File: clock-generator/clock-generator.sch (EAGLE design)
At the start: 100 parts, among them IC1 24C00TS, K2 694108106102, M1 MENTOR_12701001, U1 SN74LVC1G04DBV, U2 ADP151AUJZ, U3 ATSAMD11-QFN24, U4 SI5351C, U5 IP4234CZ6, U6 IP4234CZ6, X1 MINI-USB-SHIELD-UX60A-MB-5ST, X2 JACK2.5_SJ-2523, X4 UEXT/90

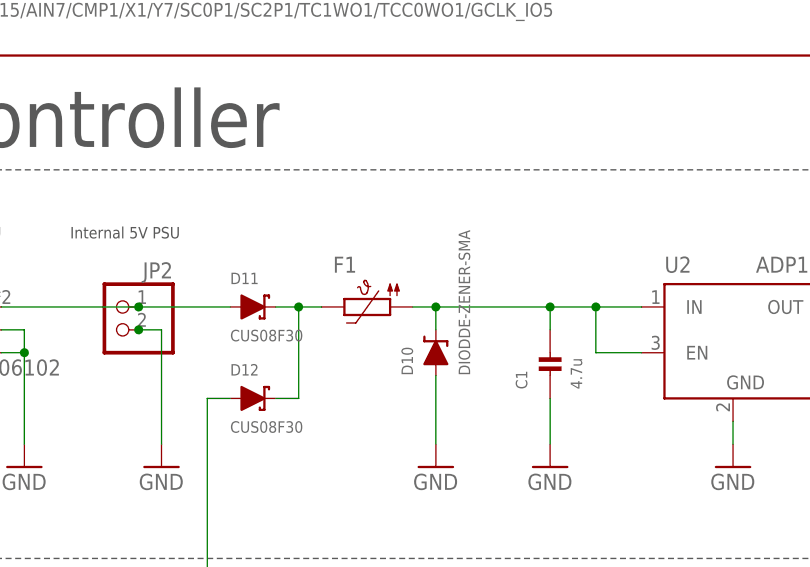
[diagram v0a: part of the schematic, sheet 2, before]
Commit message: clock-gen: Add BOM information + PDF exports of schematics
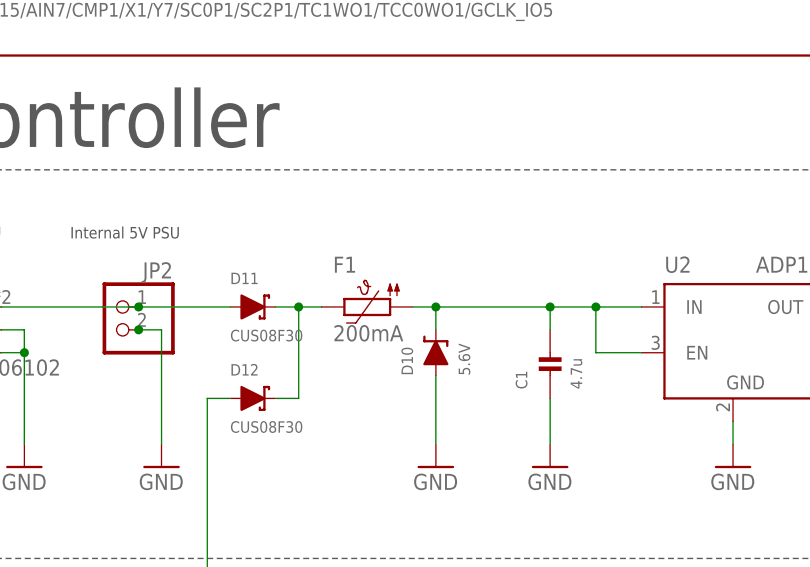
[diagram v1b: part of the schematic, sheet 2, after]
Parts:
- C1, C14, C15: CLASS (none) -> CAPACITOR; DESCRIPTION (none) -> CAP CER 4.7UF 16V X5R 0805; LINK (none) -> https://www.digikey.de/product-detail/de/samsung-electro-me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; MANUFACTURER (none) -> Samsung Electro-Mechanics; MANUFACTURERPARTNUMBER (none) -> CL21A475KOFNNNE; POPULATED (none) -> TRUE; ROHSCERTIFICATE (none) -> Bleifrei / RoHS-konform; SOURCE (none) -> DIGIKEY; SOURCEPARTNUMBER (none) -> 1276-1065-1-ND
- C10, C11, C12, C13, C8: CLASS (none) -> CAPACITOR; DESCRIPTION (none) -> CAP CER 10000PF 25V X7R 0402; LINK (none) -> https://www.digikey.de/product-detail/de/samsung-electro-me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; MANUFACTURER (none) -> Samsung Electro-Mechanics; MANUFACTURERPARTNUMBER (none) -> CL05B103KA5NNNC; POPULATED (none) -> TRUE; ROHSCERTIFICATE (none) -> Bleifrei / RoHS-konform; SOURCE (none) -> DIGIKEY; SOURCEPARTNUMBER (none) -> 1276-1057-1-ND
- C16, C17, C18, C19, C2, C20, C21, C22, C23, C24, C25, C26, C27, C28, C6, C7, C9: CLASS (none) -> CAPACITOR; DESCRIPTION (none) -> CAP CER 0.1UF 16V X7R 0603; LINK (none) -> https://www.digikey.de/product-detail/de/samsung-electro-me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; MANUFACTURER (none) -> Samsung Electro-Mechanics; MANUFACTURERPARTNUMBER (none) -> CL10B104KO8NNNC; POPULATED (none) -> TRUE; ROHSCERTIFICATE (none) -> Bleifrei / RoHS-konform; SOURCE (none) -> DIGIKEY; SOURCEPARTNUMBER (none) -> 1276-1005-1-ND
- C3: CLASS (none) -> CAPACITOR; DESCRIPTION (none) -> CAP CER 0.1UF 10V X5R 0402; LINK (none) -> https://www.digikey.de/product-detail/de/samsung-electro-me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; MANUFACTURER (none) -> Samsung Electro-Mechanics; MANUFACTURERPARTNUMBER (none) -> CL05A104MP5NNNC; POPULATED (none) -> TRUE; ROHSCERTIFICATE (none) -> Bleifrei / RoHS-konform; SOURCE (none) -> DIGIKEY; SOURCEPARTNUMBER (none) -> 1276-1443-1-ND
- C4: CLASS (none) -> CAPACITOR; DESCRIPTION (none) -> CAP CER 1UF 10V X5R 0603; LINK (none) -> https://www.digikey.de/product-detail/de/samsung-electro-me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; MANUFACTURER (none) -> Samsung Electro-Mechanics; MANUFACTURERPARTNUMBER (none) -> CL10A105KP8NNNC; POPULATED (none) -> TRUE; ROHSCERTIFICATE (none) -> Bleifrei / RoHS-konform; SOURCE (none) -> DIGIKEY; SOURCEPARTNUMBER (none) -> 1276-1182-1-ND
- C5: value 0.10n -> 10n; CLASS (none) -> CAPACITOR; DESCRIPTION (none) -> CAP CER 10000PF 25V X7R 0402; LINK (none) -> https://www.digikey.de/product-detail/de/samsung-electro-me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; MANUFACTURER (none) -> Samsung Electro-Mechanics; MANUFACTURERPARTNUMBER (none) -> CL05B103KA5NNNC; POPULATED (none) -> TRUE; ROHSCERTIFICATE (none) -> Bleifrei / RoHS-konform; SOURCE (none) -> DIGIKEY; SOURCEPARTNUMBER (none) -> 1276-1057-1-ND
- C701: DESCRIPTION CAP CER 10000PF 50V X7R 0402 -> CAP CER 10000PF 25V X7R 0402; LINK https://www.digikey.de/product-detail/de/avx-corporation/04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 -> https://www.digikey.de/product-detail/de/samsung-electro-me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; MANUFACTURER AVX Corporation -> Samsung Electro-Mechanics; MANUFACTURERPARTNUMBER 04025C103KAT2A -> CL05B103KA5NNNC; SOURCEPARTNUMBER 478-7882-1-ND -> 1276-1057-1-ND
- CLK0, CLK1, CLK2, CLK3, CLK4, CLK5, CLK6, CLK7, CLKIN: CLASS (none) -> CAPACITOR; DESCRIPTION (none) -> CONN SMA JACK R/A 50 OHM PCB; LINK (none) -> https://www.digikey.de/product-detail/de/te-connectivity-am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; MANUFACTURER (none) -> TE Connectivity AMP Connectors; MANUFACTURERPARTNUMBER (none) -> 619540-1; POPULATED (none) -> FALSE; ROHSCERTIFICATE (none) -> Bleifrei / RoHS-konform; SOURCE (none) -> DIGIKEY; SOURCEPARTNUMBER (none) -> A120734-ND
- CLK0U, CLK1U, CLK2U, CLK3U, CLK4U, CLK5U, CLK6U, CLK7U, CLKINU: CLASS (none) -> CAPACITOR; DESCRIPTION (none) -> CONN U.FL RCPT STR 50 OHM SMD; LINK (none) -> https://www.digikey.de/product-detail/de/hirose-electric-co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; MANUFACTURER (none) -> Hirose Electric Co Ltd; MANUFACTURERPARTNUMBER (none) -> U.FL-R-SMT(10); POPULATED (none) -> TRUE; ROHSCERTIFICATE (none) -> Bleifrei / RoHS-konform; SOURCE (none) -> DIGIKEY; SOURCEPARTNUMBER (none) -> H9161CT-ND
- D1, D2, D3, D4, D5, D6, D7, D8, D9: CLASS (none) -> DIODE; DESCRIPTION (none) -> SUPPRESSOR ESD 30VDC 0603 SMD; LINK (none) -> https://www.digikey.de/product-detail/de/eaton-electronics-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; MANUFACTURER (none) -> Eaton - Electronics Division; MANUFACTURERPARTNUMBER (none) -> 0603ESDA2-TR2; POPULATED (none) -> TRUE; ROHSCERTIFICATE (none) -> Bleifrei / RoHS-konform; SOURCE (none) -> DIGIKEY; SOURCEPARTNUMBER (none) -> 283-4156-1-ND
- D10: value DIODDE-ZENER-SMA -> 5.6V; CLASS (none) -> DIODE; DESCRIPTION (none) -> DIODE ZENER 5.6V 3W DO214AC; LINK (none) -> https://www.digikey.de/product-detail/de/micro-commercial-c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; MANUFACTURER (none) -> Micro Commercial Co; MANUFACTURERPARTNUMBER (none) -> 3SMAJ5919B-TP; POPULATED (none) -> TRUE; ROHSCERTIFICATE (none) -> Bleifrei / RoHS-konform; SOURCE (none) -> DIGIKEY; SOURCEPARTNUMBER (none) -> 3SMAJ5919B-TPMSCT-ND
- D11, D12: CLASS (none) -> DIODE; DESCRIPTION (none) -> DIODE SCHOTTKY 30V 800MA USC; LINK (none) -> https://www.digikey.de/product-detail/de/toshiba-semiconduc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; MANUFACTURER (none) -> Toshiba Semiconductor and Storage; MANUFACTURERPARTNUMBER (none) -> CUS08F30,H3F; POPULATED (none) -> TRUE; ROHSCERTIFICATE (none) -> Bleifrei / RoHS-konform; SOURCE (none) -> DIGIKEY; SOURCEPARTNUMBER (none) -> CUS08F30H3FCT-ND
- F1: value (none) -> 200mA; CLASS (none) -> UNKNOWN CLASS; DESCRIPTION (none) -> PTC RESET FUSE 30V 200MA 1206; LINK (none) -> https://www.digikey.de/product-detail/de/0ZCJ0020FF2E/507-1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; MANUFACTURER (none) -> Bel Fuse Inc.; MANUFACTURERPARTNUMBER (none) -> 0ZCJ0020FF2E; POPULATED (none) -> TRUE; ROHSCERTIFICATE (none) -> Bleifrei / RoHS-konform; SOURCE (none) -> DIGIKEY; SOURCEPARTNUMBER (none) -> 507-1797-1-ND
- IC1: CLASS (none) -> UNKNOWN CLASS; DESCRIPTION (none) -> IC EEPROM 2K I2C 1MHZ 8TSSOP; LINK (none) -> https://www.digikey.de/product-detail/de/microchip-technolo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; MANUFACTURER (none) -> Microchip Technology; MANUFACTURERPARTNUMBER (none) -> AT24C02C-XHM-T; POPULATED (none) -> TRUE; ROHSCERTIFICATE (none) -> Bleifrei / RoHS-konform; SOURCE (none) -> DIGIKEY; SOURCEPARTNUMBER (none) -> AT24C02C-XHM-TCT-ND
- JP1, JP2: CLASS (none) -> CONNECTOR\JUMPER; DESCRIPTION (none) -> CONN HEADER VERT 2POS 2.54MM; LINK (none) -> https://www.digikey.de/product-detail/de/PREC002SAAN-RC/S10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; MANUFACTURER (none) -> Sullins Connector Solutions; MANUFACTURERPARTNUMBER (none) -> PREC002SAAN-RC; POPULATED (none) -> TRUE; ROHSCERTIFICATE (none) -> Bleifrei / RoHS-konform; SOURCE (none) -> DIGIKEY; SOURCEPARTNUMBER (none) -> S1012EC-02-ND
- K2: DESCRIPTION Power Barrel Connector Jack 2.50mm ID (0.098"), 5.50mm OD (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 -> CONN PWR JACK 2.5X5.5MM SOLDER; LINK http://www.digikey.com/product-detail/en/wurth-electronics-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 -> http://www.digikey.de/product-detail/de/wurth-electronics-i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; MANUFACTURER Wurth Electronics Inc -> Wurth Electronics Inc.; ROHSCERTIFICATE UNKNOWN ROHS CERTIFICATE -> Bleifrei / RoHS-konform
- L2: CLASS (none) -> INDUCTOR; DESCRIPTION (none) -> FERRITE BEAD 1 KOHM 0805 1LN; LINK (none) -> https://www.digikey.de/product-detail/de/wurth-electronics-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; MANUFACTURER (none) -> Wurth Electronics Inc.; MANUFACTURERPARTNUMBER (none) -> 742792096; POPULATED (none) -> TRUE; ROHSCERTIFICATE (none) -> Bleifrei / RoHS-konform; SOURCE (none) -> DIGIKEY; SOURCEPARTNUMBER (none) -> 732-4648-1-ND
- LED1: CLASS (none) -> LED; DESCRIPTION (none) -> LED GREEN CLEAR 2PLCC SMD; LINK (none) -> https://www.digikey.de/product-detail/de/osram-opto-semicon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; MANUFACTURER (none) -> OSRAM Opto Semiconductors Inc.; MANUFACTURERPARTNUMBER (none) -> LG T67F-R1T1-24; POPULATED (none) -> TRUE; ROHSCERTIFICATE (none) -> Bleifrei / RoHS-konform; SOURCE (none) -> DIGIKEY; SOURCEPARTNUMBER (none) -> 475-3413-1-ND
- LED2: CLASS (none) -> LED; DESCRIPTION (none) -> LED YELLOW CLEAR 2PLCC SMD; LINK (none) -> https://www.digikey.de/product-detail/de/osram-opto-semicon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; MANUFACTURER (none) -> OSRAM Opto Semiconductors Inc.; MANUFACTURERPARTNUMBER (none) -> LY T676-S1T1-26-Z; POPULATED (none) -> TRUE; ROHSCERTIFICATE (none) -> Bleifrei / RoHS-konform; SOURCE (none) -> DIGIKEY; SOURCEPARTNUMBER (none) -> 475-2665-1-ND
- M1: CLASS (none) -> UNKNOWN CLASS; DESCRIPTION (none) -> NO DESCRIPTION; LINK (none) -> UNKNOWN LINK; MANUFACTURER (none) -> UNKNOWN MANUFACTURER; MANUFACTURERPARTNUMBER (none) -> UNKNOWN MANUFACTURER PART NUMBER; POPULATED (none) -> TRUE; ROHSCERTIFICATE (none) -> UNKNOWN ROHS CERTIFICATE; SOURCE (none) -> UNKNOWN SOURCE; SOURCEPARTNUMBER (none) -> UNKNOWN SOURCE PART NUMBER
- R1, R701, R703: DESCRIPTION RES 100K OHM 1/10W 1% 0603 SMD -> RES SMD 100K OHM 5%% 1/10W 0603; LINK http://www.digikey.de/product-detail/de/foo/RHM100KCFCT-ND -> https://www.digikey.de/product-detail/de/yageo/RC0603JR-071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; MANUFACTURER Rohm Semiconductor -> Yageo; MANUFACTURERPARTNUMBER MCR03ERTF1003 -> RC0603JR-07100KL; SOURCEPARTNUMBER RHM100KCFCT-ND -> 311-100KGRCT-ND
- R10, R11, R2, R3: CLASS (none) -> RESISTOR; DESCRIPTION (none) -> RES 1K OHM 1%% 1/10W 0603; LINK (none) -> https://www.digikey.de/product-detail/de/stackpole-electron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; MANUFACTURER (none) -> Stackpole Electronics Inc.; MANUFACTURERPARTNUMBER (none) -> RMCF0603FT1K00; POPULATED (none) -> TRUE; ROHSCERTIFICATE (none) -> Bleifrei / RoHS-konform; SOURCE (none) -> DIGIKEY; SOURCEPARTNUMBER (none) -> RMCF0603FT1K00CT-ND
- R12, R15: CLASS (none) -> RESISTOR; DESCRIPTION (none) -> RES 33 OHM 5%% 1/10W 0603; LINK (none) -> https://www.digikey.de/product-detail/de/stackpole-electron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; MANUFACTURER (none) -> Stackpole Electronics Inc.; MANUFACTURERPARTNUMBER (none) -> RMCF0603JT33R0; POPULATED (none) -> TRUE; ROHSCERTIFICATE (none) -> Bleifrei / RoHS-konform; SOURCE (none) -> DIGIKEY; SOURCEPARTNUMBER (none) -> RMCF0603JT33R0CT-ND
- R13, R14: DESCRIPTION RES 100K OHM 1/10W 1% 0603 SMD -> RES 330 OHM 5%% 1/10W 0603; LINK http://www.digikey.de/product-detail/de/foo/RHM100KCFCT-ND -> https://www.digikey.de/product-detail/de/stackpole-electron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; MANUFACTURER Rohm Semiconductor -> Stackpole Electronics Inc.; MANUFACTURERPARTNUMBER MCR03ERTF1003 -> RMCF0603JT330R; SOURCEPARTNUMBER RHM100KCFCT-ND -> RMCF0603JT330RCT-ND
- R16: DESCRIPTION RES 100K OHM 1/10W 1% 0603 SMD -> RES SMD 30K OHM 5%% 1/10W 0603; LINK http://www.digikey.de/product-detail/de/foo/RHM100KCFCT-ND -> https://www.digikey.de/product-detail/de/yageo/RC0603JR-073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; MANUFACTURER Rohm Semiconductor -> Yageo; MANUFACTURERPARTNUMBER MCR03ERTF1003 -> RC0603JR-0730KL; SOURCEPARTNUMBER RHM100KCFCT-ND -> 311-30KGRCT-ND
- R17: DESCRIPTION RES 100K OHM 1/10W 1% 0603 SMD -> RES SMD 47K OHM 5%% 1/10W 0603; LINK http://www.digikey.de/product-detail/de/foo/RHM100KCFCT-ND -> https://www.digikey.de/product-detail/de/yageo/RC0603JR-074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; MANUFACTURER Rohm Semiconductor -> Yageo; MANUFACTURERPARTNUMBER MCR03ERTF1003 -> RC0603JR-0747KL; SOURCEPARTNUMBER RHM100KCFCT-ND -> 311-47KGRCT-ND
- R4, R5, R6: CLASS (none) -> RESISTOR; DESCRIPTION (none) -> RES 10K OHM 5%% 1/10W 0603; LINK (none) -> https://www.digikey.de/product-detail/de/stackpole-electron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; MANUFACTURER (none) -> Stackpole Electronics Inc.; MANUFACTURERPARTNUMBER (none) -> RMCF0603JT10K0; POPULATED (none) -> TRUE; ROHSCERTIFICATE (none) -> Bleifrei / RoHS-konform; SOURCE (none) -> DIGIKEY; SOURCEPARTNUMBER (none) -> RMCF0603JT10K0CT-ND
- R7: CLASS (none) -> RESISTOR; DESCRIPTION (none) -> RES 49.9 OHM 1%% 1/10W 0603; LINK (none) -> https://www.digikey.de/product-detail/de/stackpole-electron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; MANUFACTURER (none) -> Stackpole Electronics Inc.; MANUFACTURERPARTNUMBER (none) -> RMCF0603FT49R9; POPULATED (none) -> TRUE; ROHSCERTIFICATE (none) -> Bleifrei / RoHS-konform; SOURCE (none) -> DIGIKEY; SOURCEPARTNUMBER (none) -> RMCF0603FT49R9CT-ND
- R8, R9: CLASS (none) -> RESISTOR; DESCRIPTION (none) -> RES SMD 510K OHM 1%% 1/10W 0603; LINK (none) -> https://www.digikey.de/product-detail/de/yageo/RC0603FR-075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; MANUFACTURER (none) -> Yageo; MANUFACTURERPARTNUMBER (none) -> RC0603FR-07510KL; POPULATED (none) -> TRUE; ROHSCERTIFICATE (none) -> Bleifrei / RoHS-konform; SOURCE (none) -> DIGIKEY; SOURCEPARTNUMBER (none) -> 311-510KHRCT-ND
- TC1: CLASS (none) -> UNKNOWN CLASS; DESCRIPTION (none) -> NO DESCRIPTION; LINK (none) -> UNKNOWN LINK; MANUFACTURER (none) -> UNKNOWN MANUFACTURER; MANUFACTURERPARTNUMBER (none) -> UNKNOWN MANUFACTURER PART NUMBER; POPULATED (none) -> FALSE; ROHSCERTIFICATE (none) -> UNKNOWN ROHS CERTIFICATE; SOURCE (none) -> UNKNOWN SOURCE; SOURCEPARTNUMBER (none) -> UNKNOWN SOURCE PART NUMBER
- U1: CLASS (none) -> IC; DESCRIPTION (none) -> IC INVERTER 1CH 1-INP SOT23-5; LINK (none) -> https://www.digikey.de/product-detail/de/texas-instruments/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; MANUFACTURER (none) -> Texas Instruments; MANUFACTURERPARTNUMBER (none) -> SN74LVC1G04DBVR; POPULATED (none) -> TRUE; ROHSCERTIFICATE (none) -> Bleifrei / RoHS-konform; SOURCE (none) -> DIGIKEY; SOURCEPARTNUMBER (none) -> 296-11599-1-ND
- U2: CLASS (none) -> IC; DESCRIPTION (none) -> IC REG LINEAR 3V 200MA TSOT5; LINK (none) -> https://www.digikey.de/product-detail/de/analog-devices-inc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; MANUFACTURER (none) -> Analog Devices Inc.; MANUFACTURERPARTNUMBER (none) -> ADP151AUJZ-3.0-R7; POPULATED (none) -> TRUE; ROHSCERTIFICATE (none) -> Bleifrei / RoHS-konform; SOURCE (none) -> DIGIKEY; SOURCEPARTNUMBER (none) -> ADP151AUJZ-3.0-R7CT-ND
- U3: CLASS (none) -> IC; DESCRIPTION (none) -> IC MCU 32BIT 16KB FLASH 24QFN; LINK (none) -> https://www.digikey.de/product-detail/de/microchip-technolo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; MANUFACTURER (none) -> Microchip Technology; MANUFACTURERPARTNUMBER (none) -> ATSAMD11D14A-MUT; POPULATED (none) -> TRUE; ROHSCERTIFICATE (none) -> Bleifrei / RoHS-konform; SOURCE (none) -> DIGIKEY; SOURCEPARTNUMBER (none) -> ATSAMD11D14A-MUTCT-ND
- U4: CLASS (none) -> IC; DESCRIPTION (none) -> IC CLK GENERATOR 200MHZ 20QFN; LINK (none) -> https://www.digikey.de/product-detail/de/silicon-labs/SI535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; MANUFACTURER (none) -> Silicon Labs; MANUFACTURERPARTNUMBER (none) -> SI5351C-B-GMR; POPULATED (none) -> TRUE; ROHSCERTIFICATE (none) -> Bleifrei / RoHS-konform; SOURCE (none) -> DIGIKEY; SOURCEPARTNUMBER (none) -> 336-5160-6-ND
- U5, U6: CLASS (none) -> IC; DESCRIPTION (none) -> TVS DIODE 5.5V 6TSOP; LINK (none) -> https://www.digikey.de/product-detail/de/nexperia-usa-inc/I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; MANUFACTURER (none) -> Nexperia USA Inc.; MANUFACTURERPARTNUMBER (none) -> IP4234CZ6,125; POPULATED (none) -> TRUE; ROHSCERTIFICATE (none) -> Bleifrei / RoHS-konform; SOURCE (none) -> DIGIKEY; SOURCEPARTNUMBER (none) -> 1727-4717-1-ND
- X1: CLASS (none) -> CONNECTOR; DESCRIPTION (none) -> CONN RCPT USB2.0 MINI B SMD R/A; LINK (none) -> https://www.digikey.de/product-detail/de/hirose-electric-co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; MANUFACTURER (none) -> Hirose Electric Co Ltd; MANUFACTURERPARTNUMBER (none) -> UX60A-MB-5ST; POPULATED (none) -> TRUE; ROHSCERTIFICATE (none) -> Bleifrei / RoHS-konform; SOURCE (none) -> DIGIKEY; SOURCEPARTNUMBER (none) -> H2961CT-ND
- X2: CLASS (none) -> CONNECTOR; DESCRIPTION (none) -> CONN JACK STEREO 2.5MM SMD R/A; LINK (none) -> https://www.digikey.de/product-detail/de/cui-inc/SJ-2523-SM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; MANUFACTURER (none) -> CUI Inc.; MANUFACTURERPARTNUMBER (none) -> SJ-2523-SMT-TR; POPULATED (none) -> TRUE; ROHSCERTIFICATE (none) -> Bleifrei / RoHS-konform; SOURCE (none) -> DIGIKEY; SOURCEPARTNUMBER (none) -> CP-2523SJCT-ND
- X3: CLASS (none) -> CONNECTOR; DESCRIPTION (none) -> NO DESCRIPTION; LINK (none) -> UNKNOWN LINK; MANUFACTURER (none) -> UNKNOWN MANUFACTURER; MANUFACTURERPARTNUMBER (none) -> UNKNOWN MANUFACTURER PART NUMBER; POPULATED (none) -> FALSE; ROHSCERTIFICATE (none) -> UNKNOWN ROHS CERTIFICATE; SOURCE (none) -> UNKNOWN SOURCE; SOURCEPARTNUMBER (none) -> UNKNOWN SOURCE PART NUMBER
- X4: CLASS (none) -> CONNECTOR; DESCRIPTION (none) -> CONN HEADER VERT 10POS 2.54MM; LINK (none) -> https://www.digikey.de/product-detail/de/on-shore-technolog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; MANUFACTURER (none) -> On Shore Technology Inc.; MANUFACTURERPARTNUMBER (none) -> 302-S101; POPULATED (none) -> TRUE; ROHSCERTIFICATE (none) -> Bleifrei / RoHS-konform; SOURCE (none) -> DIGIKEY; SOURCEPARTNUMBER (none) -> ED1543-ND
- XO1: CLASS (none) -> CONNECTOR; DESCRIPTION (none) -> XTAL OSC VCTCXO 10.0000MHZ LVCMO; LINK (none) -> https://www.digikey.de/product-detail/de/connor-winfield/T6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; MANUFACTURER (none) -> Connor-Winfield; MANUFACTURERPARTNUMBER (none) -> T604-010.0M; POPULATED (none) -> TRUE; ROHSCERTIFICATE (none) -> Bleifrei / RoHS-konform; SOURCE (none) -> DIGIKEY; SOURCEPARTNUMBER (none) -> CW769CT-ND

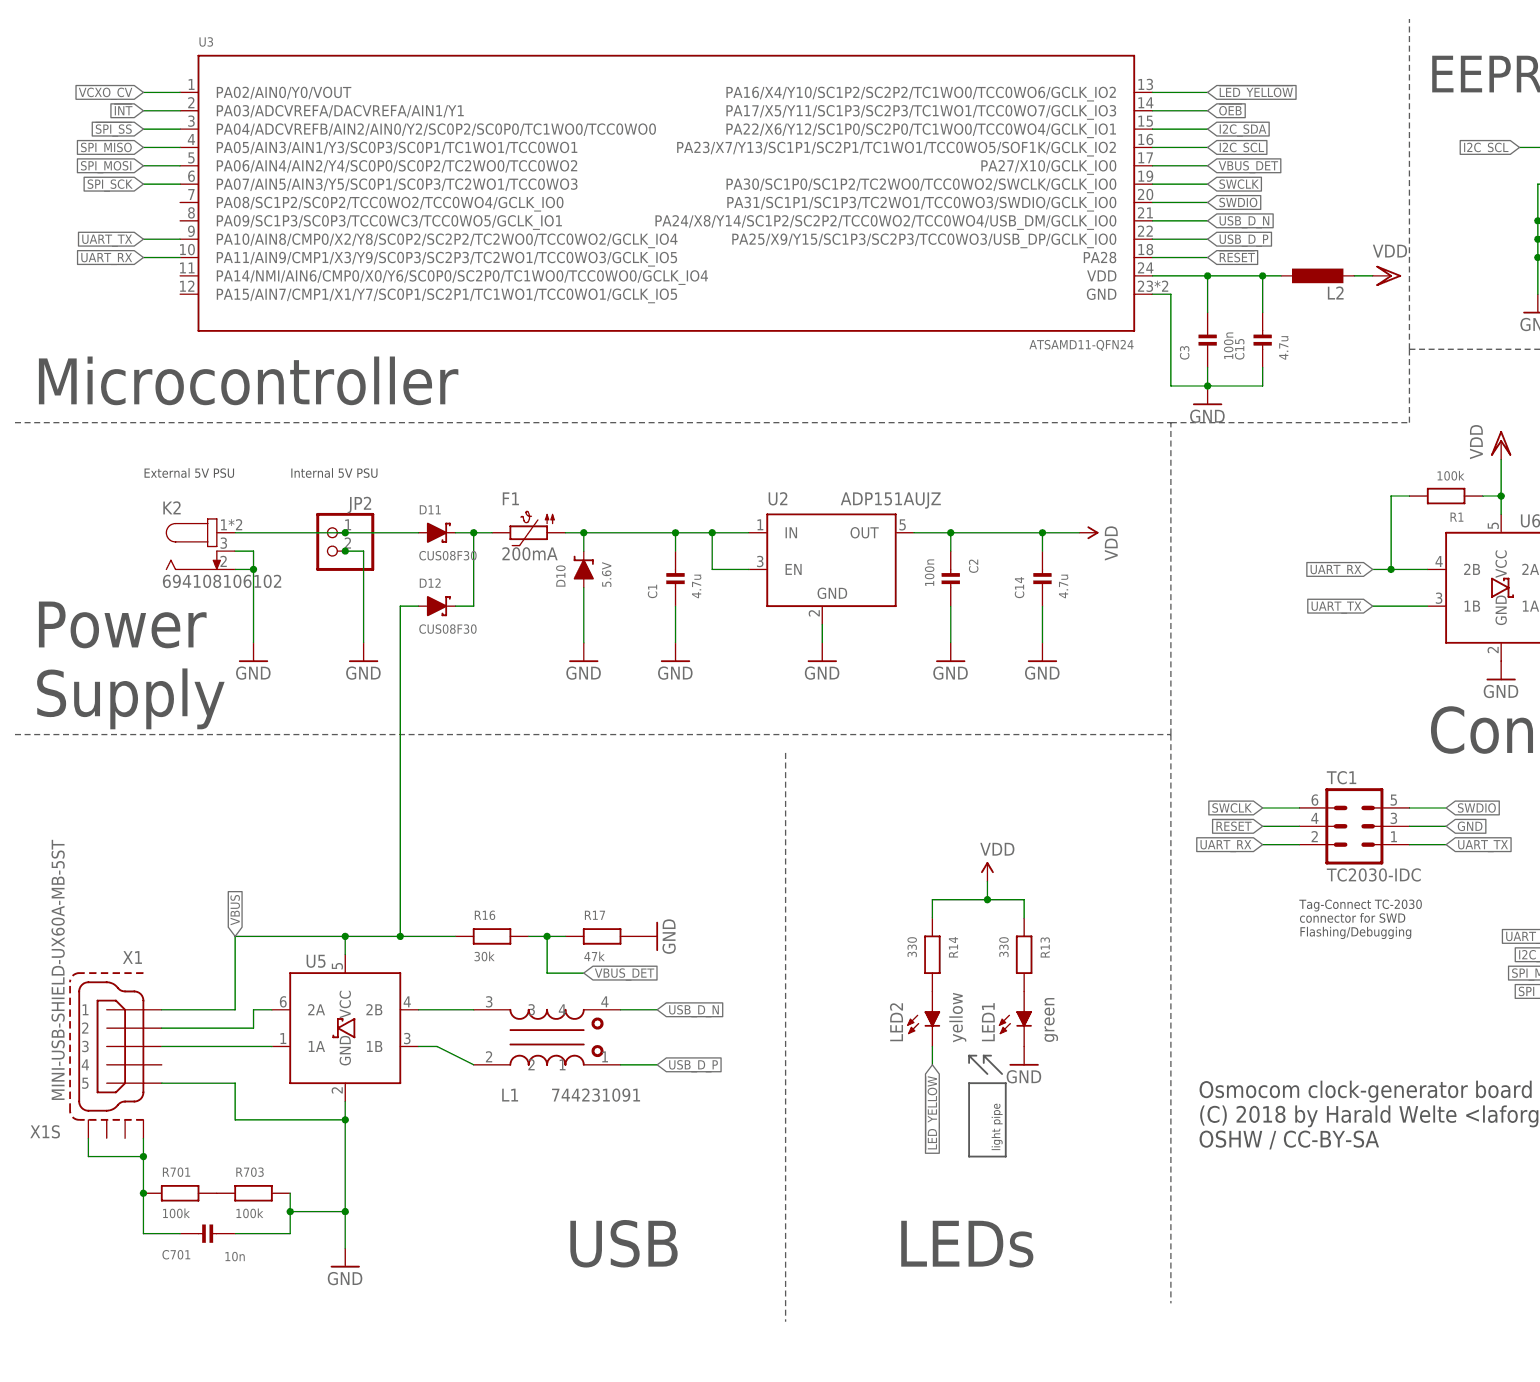
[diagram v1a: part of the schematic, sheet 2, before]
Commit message: WIP: click-generator: Replace U3 (so far SAMD11) with SAMD21
Closes: OS#3856
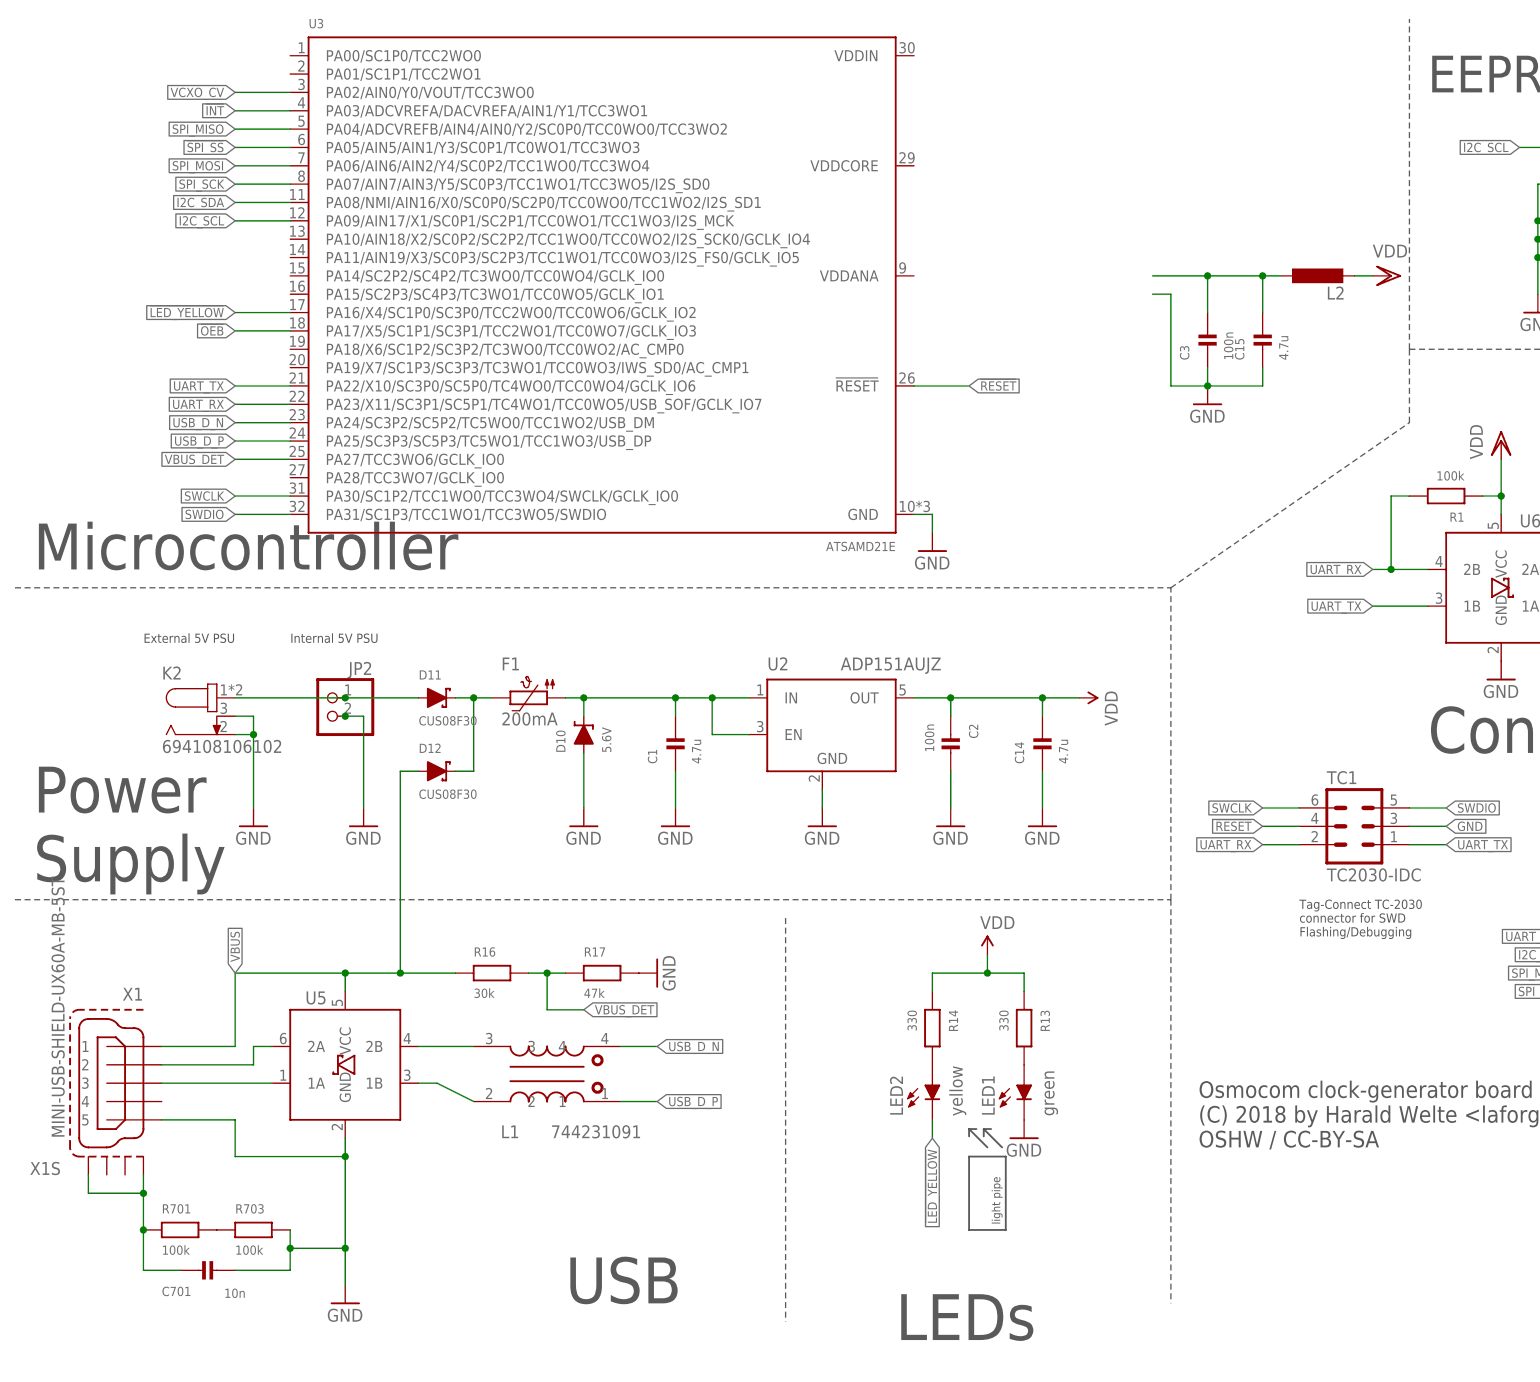
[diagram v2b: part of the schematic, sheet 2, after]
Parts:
- U3: value ATSAMD11-QFN24 -> ATSAMD21E; device atmel-arm:ATSAMD11-QFN24 -> atmel-arm:ATSAMD21E; CLASS IC -> (none); DESCRIPTION IC MCU 32BIT 16KB FLASH 24QFN -> (none); LINK https://www.digikey.de/product-detail/de/microchip-technolo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 -> (none); MANUFACTURER Microchip Technology -> (none); MANUFACTURERPARTNUMBER ATSAMD11D14A-MUT -> (none); POPULATED TRUE -> (none); ROHSCERTIFICATE Bleifrei / RoHS-konform -> (none); SOURCE DIGIKEY -> (none); SOURCEPARTNUMBER ATSAMD11D14A-MUTCT-ND -> (none)
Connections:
- net !INT: now also U3.PA03/ADCVREFA/DACVREFA/AIN1/Y1/TCC3WO1; no longer U3.PA03/ADCVREFA/DACVREFA/AIN1/Y1
- net !LED_YELLOW: now also U3.PA16/X4/SC1P0/SC3P0/TCC2WO0/TCC0WO6/GCLK_IO2; no longer U3.PA16/X4/Y10/SC1P2/SC2P2/TC1WO0/TCC0WO6/GCLK_IO2
- net !OEB: now also U3.PA17/X5/SC1P1/SC3P1/TCC2WO1/TCC0WO7/GCLK_IO3; no longer U3.PA17/X5/Y11/SC1P3/SC2P3/TC1WO1/TCC0WO7/GCLK_IO3
- net !RESET: now also U3.!RESET; no longer U3.PA28
- net !SPI_SS: now also U3.PA05/AIN5/AIN1/Y3/SC0P1/TC0WO1/TCC3WO3; no longer U3.PA04/ADCVREFB/AIN2/AIN0/Y2/SC0P2/SC0P0/TC1WO0/TCC0WO0
- net I2C_SCL: now also U3.PA09/AIN17/X1/SC0P1/SC2P1/TCC0WO1/TCC1WO3/I2S_MCK; no longer U3.PA23/X7/Y13/SC1P1/SC2P1/TC1WO1/TCC0WO5/SOF1K/GCLK_IO2
- net I2C_SDA: now also U3.PA08/NMI/AIN16/X0/SC0P0/SC2P0/TCC0WO0/TCC1WO2/I2S_SD1; no longer U3.PA22/X6/Y12/SC1P0/SC2P0/TC1WO0/TCC0WO4/GCLK_IO1
- net N$13: no longer U3.VDD
- net SPI_MISO: now also U3.PA04/ADCVREFB/AIN4/AIN0/Y2/SC0P0/TCC0WO0/TCC3WO2; no longer U3.PA05/AIN3/AIN1/Y3/SC0P3/SC0P1/TC1WO1/TCC0WO1
- net SPI_MOSI: now also U3.PA06/AIN6/AIN2/Y4/SC0P2/TCC1WO0/TCC3WO4; no longer U3.PA06/AIN4/AIN2/Y4/SC0P0/SC0P2/TC2WO0/TCC0WO2
- net SPI_SCK: now also U3.PA07/AIN7/AIN3/Y5/SC0P3/TCC1WO1/TCC3WO5/I2S_SD0; no longer U3.PA07/AIN5/AIN3/Y5/SC0P1/SC0P3/TC2WO1/TCC0WO3
- net SWCLK: now also U3.PA30/SC1P2/TCC1WO0/TCC3WO4/SWCLK/GCLK_IO0; no longer U3.PA30/SC1P0/SC1P2/TC2WO0/TCC0WO2/SWCLK/GCLK_IO0
- net SWDIO: now also U3.PA31/SC1P3/TCC1WO1/TCC3WO5/SWDIO; no longer U3.PA31/SC1P1/SC1P3/TC2WO1/TCC0WO3/SWDIO/GCLK_IO0
- net UART_RX: now also U3.PA23/X11/SC3P1/SC5P1/TC4WO1/TCC0WO5/USB_SOF/GCLK_IO7; no longer U3.PA11/AIN9/CMP1/X3/Y9/SC0P3/SC2P3/TC2WO1/TCC0WO3/GCLK_IO5
- net UART_TX: now also U3.PA22/X10/SC3P0/SC5P0/TC4WO0/TCC0WO4/GCLK_IO6; no longer U3.PA10/AIN8/CMP0/X2/Y8/SC0P2/SC2P2/TC2WO0/TCC0WO2/GCLK_IO4
- net USB_D_N: now also U3.PA24/SC3P2/SC5P2/TC5WO0/TCC1WO2/USB_DM; no longer U3.PA24/X8/Y14/SC1P2/SC2P2/TCC0WO2/TCC0WO4/USB_DM/GCLK_IO0
- net USB_D_P: now also U3.PA25/SC3P3/SC5P3/TC5WO1/TCC1WO3/USB_DP; no longer U3.PA25/X9/Y15/SC1P3/SC2P3/TCC0WO3/USB_DP/GCLK_IO0
- net VBUS_DET: now also U3.PA27/TCC3WO6/GCLK_IO0; no longer U3.PA27/X10/GCLK_IO0
- net VCXO_CV: now also U3.PA02/AIN0/Y0/VOUT/TCC3WO0; no longer U3.PA02/AIN0/Y0/VOUT
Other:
- moved on the sheet: C1, C14, C2, C701, D10, D11, D12, F1, JP2, K2, L1, LED1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
